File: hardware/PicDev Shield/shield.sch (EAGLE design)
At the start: 7 parts

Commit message: Finished shield
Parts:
- removed JP5: (no value), pinhead:PINHD-2X10
- added OV2640: (no value), custom:PINHD-2X10
- JP1, JP3: device pinhead:PINHD-1X18/90 -> custom:PINHD-1X18/90
- JP2, JP4: device pinhead:PINHD-1X16/90 -> custom:PINHD-1X16/90
- renumbered JP7 to ENC28J60
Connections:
- removed net 5V: JP1.1, JP3.18
- new net +5V: JP3.18, X1-1.KL
- new net GND2: JP3.1, OV2640.2, X1-2.KL
- net +3V3: now also OV2640.1; no longer JP1.11, JP2.10, JP2.3, JP3.7, JP4.9
- net GND: now also ENC28J60.2; no longer JP1.10, JP2.4, JP2.9, JP3.1, JP3.10
- net RB0: now also OV2640.8
- net RB10: now also OV2640.14
- net RB11: now also OV2640.13
- net RB12: now also OV2640.12
- net RB13: now also OV2640.11
- net RB14: now also OV2640.10
- net RB15: now also OV2640.9
- net RB2: now also OV2640.18
- net RB3: now also OV2640.20
- net RB4: now also OV2640.19
- net RB5: now also OV2640.17
- net RB8: now also OV2640.16
- net RB9: now also OV2640.15
- net RD0: now also OV2640.7
- net RD10: now also OV2640.3
- net RD11: now also OV2640.5
- net RD9: now also OV2640.4
- net RE0: now also ENC28J60.8
- net RE1: now also ENC28J60.7
- net RE2: now also ENC28J60.6
- net RE3: now also ENC28J60.4
- net RE4: now also ENC28J60.3
- net RE5: no longer ENC28J60.1
- net RF0: now also ENC28J60.10
- net RF1: now also ENC28J60.9
- net RF3: now also OV2640.6
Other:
- note added: "/CS"
- note added: "/INT"
- note added: "/RESET"
- note added: "CLKOUT"
- note added: "D0"
- note added: "D1"
- note added: "D2"
- note added: "D3"
- note added: "D4"
- note added: "D5"
- note added: "D6"
- note added: "D7"
- note added: "GND"
- note added: "HREFX"
- note added: "MISO"
- note added: "MOSI"
- note added: "PCLK"
- note added: "PWDN"
- note added: "RESET"
- note added: "SCK"
- note added: "SCL"
- note added: "SDA"
- note added: "VCC"
- note added: "VSYNC"
- note added: "XVCLK"
- note added: "Y0"
- note added: "Y1"
- note removed: "Vcap"

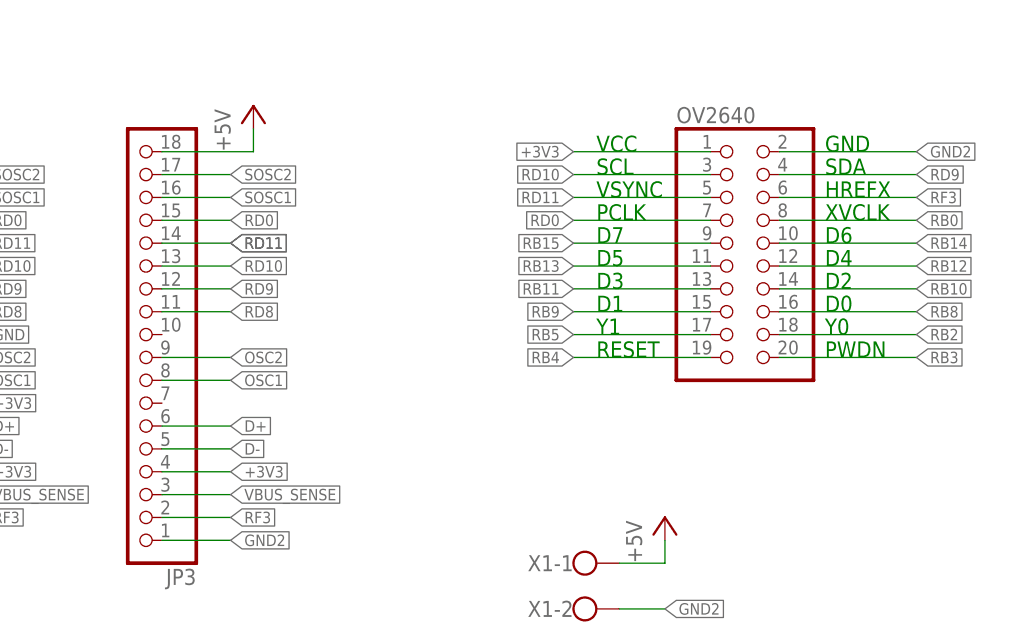
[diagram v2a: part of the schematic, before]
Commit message: I2C config/new camera functions/extra debugging functions/terminal update - I2C does not work atm, but camera can be activated/deactivated.
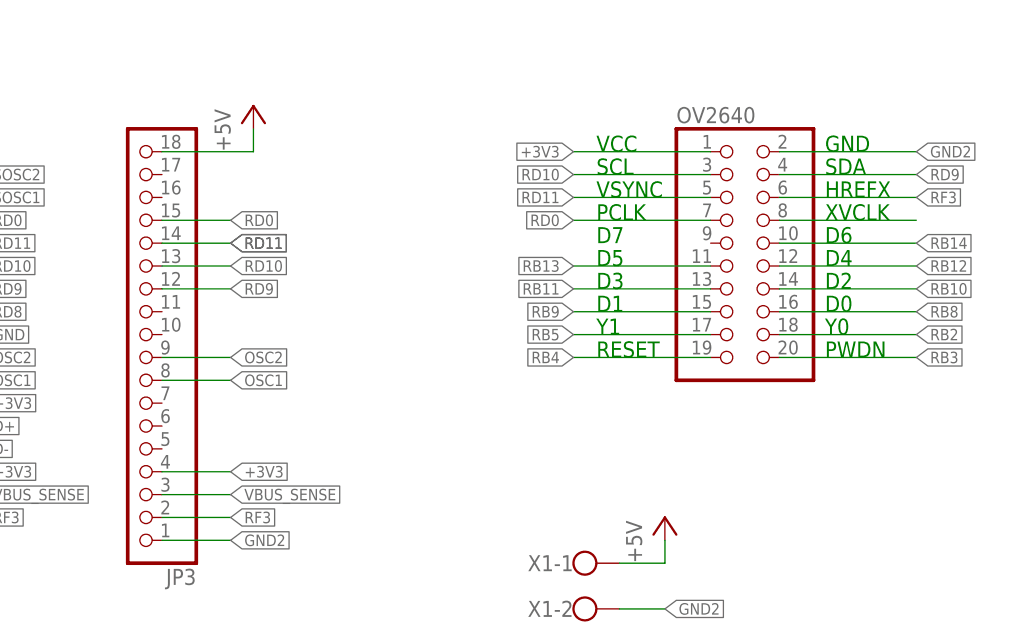
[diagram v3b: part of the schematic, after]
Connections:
- removed net D+: JP3.6
- removed net D-: JP3.5
- removed net RD8: JP3.11
- removed net SOSC1: JP3.16
- removed net SOSC2: JP3.17
- net RB15: no longer OV2640.9
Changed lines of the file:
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@@
 <?xml version="1.0" encoding="utf-8"?>
 <!DOCTYPE eagle SYSTEM "eagle.dtd">
-<eagle version="6.6.0">
+<eagle version="6.5.0">
 <drawing>
 <settings>
@@
 <pinref part="JP2" gate="A" pin="14"/>
 </segment>
-<segment>
-<wire x1="165.1" y1="83.82" x2="180.34" y2="83.82" width="0.1524" layer="91"/>
-<label x="165.1" y="83.82" size="1.27" layer="95" rot="R180" xref="yes"/>
-<pinref part="OV2640" gate="A" pin="9"/>
-</segment>
 </net>
 <net name="RF3" class="0">
@@
 <wire x1="99.06" y1="76.2" x2="93.98" y2="76.2" width="0.1524" layer="91"/>
 <label x="99.06" y="76.2" size="1.27" layer="95" xref="yes"/>
-</segment>
-<segment>
-<wire x1="127" y1="76.2" x2="119.38" y2="76.2" width="0.1524" layer="91"/>
-<label x="127" y="76.2" size="1.27" layer="95" xref="yes"/>
-<pinref part="JP3" gate="A" pin="11"/>
 </segment>
 </net>
@@
 <net name="SOSC1" class="0">
 <segment>
-<wire x1="127" y1="88.9" x2="119.38" y2="88.9" width="0.1524" layer="91"/>
-<label x="127" y="88.9" size="1.27" layer="95" xref="yes"/>
-<pinref part="JP3" gate="A" pin="16"/>
-</segment>
-<segment>
 <wire x1="99.06" y1="88.9" x2="93.98" y2="88.9" width="0.1524" layer="91"/>
 <label x="99.06" y="88.9" size="1.27" layer="95" xref="yes"/>
@@
 <net name="SOSC2" class="0">
 <segment>
-<wire x1="127" y1="91.44" x2="119.38" y2="91.44" width="0.1524" layer="91"/>
-<label x="127" y="91.44" size="1.27" layer="95" xref="yes"/>
-<pinref part="JP3" gate="A" pin="17"/>
-</segment>
-<segment>
 <wire x1="99.06" y1="91.44" x2="93.98" y2="91.44" width="0.1524" layer="91"/>
 <label x="99.06" y="91.44" size="1.27" layer="95" xref="yes"/>
@@
 <label x="99.06" y="63.5" size="1.27" layer="95" xref="yes"/>
 </segment>
-<segment>
-<wire x1="127" y1="63.5" x2="119.38" y2="63.5" width="0.1524" layer="91"/>
-<label x="127" y="63.5" size="1.27" layer="95" xref="yes"/>
-<pinref part="JP3" gate="A" pin="6"/>
-</segment>
 </net>
 <net name="D-" class="0">
@@
 <wire x1="99.06" y1="60.96" x2="93.98" y2="60.96" width="0.1524" layer="91"/>
 <label x="99.06" y="60.96" size="1.27" layer="95" xref="yes"/>
-</segment>
-<segment>
-<wire x1="127" y1="60.96" x2="119.38" y2="60.96" width="0.1524" layer="91"/>
-<label x="127" y="60.96" size="1.27" layer="95" xref="yes"/>
-<pinref part="JP3" gate="A" pin="5"/>
 </segment>
 </net>
@@
 <wire x1="27.94" y1="53.34" x2="20.32" y2="53.34" width="0.1524" layer="91"/>
 <pinref part="JP1" gate="A" pin="17"/>
-<label x="203.2" y="86.36" size="1.27" layer="95" xref="yes"/>
-</segment>
-<segment>
+</segment>
+<segment>

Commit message: Beta
Beta
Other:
- note added: "RST"
- note removed: "RESET"
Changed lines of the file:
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@@
 <?xml version="1.0" encoding="utf-8"?>
 <!DOCTYPE eagle SYSTEM "eagle.dtd">
-<eagle version="6.5.0">
+<eagle version="6.6.0">
 <drawing>
 <settings>
@@
 <text x="167.64" y="76.2" size="1.778" layer="91">D1</text>
 <text x="167.64" y="73.66" size="1.778" layer="91">Y1</text>
-<text x="167.64" y="71.12" size="1.778" layer="91">RESET</text>
+<text x="167.64" y="71.12" size="1.778" layer="91">RST</text>
 </plain>
 <instances>
@@
 <pinref part="OV2640" gate="A" pin="11"/>
 </segment>
+<segment>
+<wire x1="165.1" y1="83.82" x2="180.34" y2="83.82" width="0.1524" layer="91"/>
+</segment>
 </net>
 <net name="RB14" class="0">
@@
 <label x="83.82" y="20.32" size="1.27" layer="95" rot="R270" xref="yes"/>
 <pinref part="JP2" gate="A" pin="13"/>
+<label x="83.82" y="45.72" size="1.27" layer="95" rot="R270" xref="yes"/>
 </segment>
 <segment>
@@
 <label x="86.36" y="20.32" size="1.27" layer="95" rot="R270" xref="yes"/>
 <pinref part="JP2" gate="A" pin="14"/>
+<label x="203.2" y="86.36" size="1.27" layer="95" xref="yes"/>
+<label x="86.36" y="45.72" size="1.27" layer="95" rot="R270" xref="yes"/>
 </segment>
 </net>
@@
 <wire x1="27.94" y1="53.34" x2="20.32" y2="53.34" width="0.1524" layer="91"/>
 <pinref part="JP1" gate="A" pin="17"/>
+<label x="165.1" y="83.82" size="1.27" layer="95" rot="R180" xref="yes"/>
 </segment>
 <segment>
@@
 <segment>
 <wire x1="83.82" y1="45.72" x2="83.82" y2="50.8" width="0.1524" layer="91"/>
-<label x="83.82" y="45.72" size="1.27" layer="95" rot="R270" xref="yes"/>
-</segment>
-</net>
-<net name="N$12" class="0">
-<segment>
-<wire x1="86.36" y1="45.72" x2="86.36" y2="50.8" width="0.1524" layer="91"/>
-<label x="86.36" y="45.72" size="1.27" layer="95" rot="R270" xref="yes"/>
 </segment>
 </net>
@@
 </segment>
 </net>
+<net name="N$2" class="0">
+<segment>
+<wire x1="86.36" y1="45.72" x2="86.36" y2="50.8" width="0.1524" layer="91"/>
+</segment>
+</net>
